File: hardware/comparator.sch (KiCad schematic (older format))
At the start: 11 parts

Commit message: more work on tdr schematic
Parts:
- U?: symbol synth_lib:SY89321L -> tdr-rescue:SY89321L-synth_lib
- U?: symbol synth_lib:ADCMP580 -> tdr-rescue:ADCMP580-synth_lib
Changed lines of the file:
@@
 $EndDescr
 $Comp
-L synth_lib:ADCMP580 U?
+L tdr-rescue:ADCMP580-synth_lib U?
 U 1 1 5BC42930
 P 5200 3300
@@
 	5250 3950 5250 4600
 $Comp
-L synth_lib:SY89321L U?
+L tdr-rescue:SY89321L-synth_lib U?
 U 1 1 5BC3E45C
 P 8650 3300

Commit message: work on tdr schematic..
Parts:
- U?: symbol tdr-rescue:SY89321L-synth_lib -> tdr-rescue:SY89321L-synth_lib-tdr-rescue
- U?: symbol tdr-rescue:ADCMP580-synth_lib -> tdr-rescue:ADCMP580-synth_lib-tdr-rescue
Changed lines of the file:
@@
 $Descr A4 11693 8268
 encoding utf-8
-Sheet 4 9
+Sheet 4 8
 Title ""
 Date ""
@@
 $EndDescr
 $Comp
-L tdr-rescue:ADCMP580-synth_lib U?
+L tdr-rescue:ADCMP580-synth_lib-tdr-rescue U?
 U 1 1 5BC42930
 P 5200 3300
@@
 	5250 3950 5250 4600
 $Comp
-L tdr-rescue:SY89321L-synth_lib U?
+L tdr-rescue:SY89321L-synth_lib-tdr-rescue U?
 U 1 1 5BC3E45C
 P 8650 3300

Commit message: footprint assignment
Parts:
- C401, C402, C403, C404, C405: renamed from C?; footprint (none) -> Capacitors_SMD:C_0402
- R401, R402, R403, R404: renamed from R?; footprint (none) -> Resistors_SMD:R_0402
- U401: renamed from U?; footprint (none) -> Housings_DFN_QFN:QFN-16-1EP_3x3mm_Pitch0.5mm
- U402: renamed from U?; footprint (none) -> Housings_DFN_QFN:DFN-8-1EP_2x2mm_Pitch0.5mm
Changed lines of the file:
@@
 $EndDescr
 $Comp
-L tdr-rescue:ADCMP580-synth_lib-tdr-rescue U?
+L tdr-rescue:ADCMP580-synth_lib-tdr-rescue U401
 U 1 1 5BC42930
 P 5200 3300
-F 0 "U?" H 4500 3900 50  0000 L CNN
+F 0 "U401" H 4500 3900 50  0000 L CNN
 F 1 "ADCMP580" H 4500 3800 50  0000 L CNN
-F 2 "" H 4300 3800 50  0001 C CNN
+F 2 "Housings_DFN_QFN:QFN-16-1EP_3x3mm_Pitch0.5mm" H 4300 3800 50  0001 C CNN
 F 3 "" H 4300 3800 50  0001 C CNN
 	1    5200 3300
@@
 $EndComp
 $Comp
-L power:+5VA #PWR?
+L power:+5VA #PWR0211
 U 1 1 5BC42937
 P 5050 2100
-F 0 "#PWR?" H 5050 1950 50  0001 C CNN
+F 0 "#PWR0211" H 5050 1950 50  0001 C CNN
 F 1 "+5VA" V 5050 2350 50  0000 C CNN
 F 2 "" H 5050 2100 50  0001 C CNN
@@
 $EndComp
 $Comp
-L power:-5VA #PWR?
+L power:-5VA #PWR0212
 U 1 1 5BC4293D
 P 5350 2100
-F 0 "#PWR?" H 5350 2200 50  0001 C CNN
+F 0 "#PWR0212" H 5350 2200 50  0001 C CNN
 F 1 "-5VA" H 5365 2273 50  0000 C CNN
 F 2 "" H 5350 2100 50  0001 C CNN
@@
 $EndComp
 $Comp
-L power:GND #PWR?
+L power:GND #PWR0213
 U 1 1 5BC42943
 P 5350 4000
-F 0 "#PWR?" H 5350 3750 50  0001 C CNN
+F 0 "#PWR0213" H 5350 3750 50  0001 C CNN
 F 1 "GND" H 5355 3827 50  0000 C CNN
 F 2 "" H 5350 4000 50  0001 C CNN
@@
 	5350 3950 5350 4000
 $Comp
-L power:GND #PWR?
+L power:GND #PWR0214
 U 1 1 5BC4294A
 P 5450 4000
-F 0 "#PWR?" H 5450 3750 50  0001 C CNN
+F 0 "#PWR0214" H 5450 3750 50  0001 C CNN
 F 1 "GND" H 5455 3827 50  0000 C CNN
 F 2 "" H 5450 4000 50  0001 C CNN
@@
 	5450 4000 5450 3950
 $Comp
-L power:GND #PWR?
+L power:GND #PWR0215
 U 1 1 5BC42951
 P 5900 3450
-F 0 "#PWR?" H 5900 3200 50  0001 C CNN
+F 0 "#PWR0215" H 5900 3200 50  0001 C CNN
 F 1 "GND" V 5905 3322 50  0000 R CNN
 F 2 "" H 5900 3450 50  0001 C CNN
@@
 	5900 3450 5850 3450
 $Comp
-L power:GND #PWR?
+L power:GND #PWR0216
 U 1 1 5BC42958
 P 5900 3150
-F 0 "#PWR?" H 5900 2900 50  0001 C CNN
+F 0 "#PWR0216" H 5900 2900 50  0001 C CNN
 F 1 "GND" V 5905 3022 50  0000 R CNN
 F 2 "" H 5900 3150 50  0001 C CNN
@@
 	5900 3150 5850 3150
 $Comp
-L power:GND #PWR?
+L power:GND #PWR0217
 U 1 1 5BC4295F
 P 5150 2600
-F 0 "#PWR?" H 5150 2350 50  0001 C CNN
+F 0 "#PWR0217" H 5150 2350 50  0001 C CNN
 F 1 "GND" V 5200 2600 50  0001 C CNN
 F 2 "" H 5150 2600 50  0001 C CNN
@@
 $EndComp
 $Comp
-L Device:C_Small C?
+L Device:C_Small C401
 U 1 1 5BC42965
 P 4750 2350
-F 0 "C?" H 4350 2400 50  0000 L CNN
+F 0 "C401" H 4350 2400 50  0000 L CNN
 F 1 ".01 uF" H 4350 2300 50  0000 L CNN
-F 2 "" H 4750 2350 50  0001 C CNN
+F 2 "Capacitors_SMD:C_0402" H 4750 2350 50  0001 C CNN
 F 3 "~" H 4750 2350 50  0001 C CNN
 	1    4750 2350
@@
 	5050 2200 5050 2650
 $Comp
-L power:GND #PWR?
+L power:GND #PWR0218
 U 1 1 5BC42971
 P 4750 2500
-F 0 "#PWR?" H 4750 2250 50  0001 C CNN
+F 0 "#PWR0218" H 4750 2250 50  0001 C CNN
 F 1 "GND" H 4750 2350 50  0000 C CNN
 F 2 "" H 4750 2500 50  0001 C CNN
@@
 	4750 2500 4750 2450
 $Comp
-L power:+5VA #PWR?
+L power:+5VA #PWR0219
 U 1 1 5BC42978
 P 4700 4050
-F 0 "#PWR?" H 4700 3900 50  0001 C CNN
+F 0 "#PWR0219" H 4700 3900 50  0001 C CNN
 F 1 "+5VA" V 4700 4300 50  0000 C CNN
 F 2 "" H 4700 4050 50  0001 C CNN
@@
 	5050 4050 4800 4050
 $Comp
-L Device:C_Small C?
+L Device:C_Small C402
 U 1 1 5BC42980
 P 4800 4200
-F 0 "C?" H 4892 4246 50  0000 L CNN
+F 0 "C402" H 4892 4246 50  0000 L CNN
 F 1 ".01 uF" H 4892 4155 50  0000 L CNN
-F 2 "" H 4800 4200 50  0001 C CNN
+F 2 "Capacitors_SMD:C_0402" H 4800 4200 50  0001 C CNN
 F 3 "~" H 4800 4200 50  0001 C CNN
 	1    4800 4200
@@
 $EndComp
 $Comp
-L power:GND #PWR?
+L power:GND #PWR0220
 U 1 1 5BC42987
 P 4800 4350
-F 0 "#PWR?" H 4800 4100 50  0001 C CNN
+F 0 "#PWR0220" H 4800 4100 50  0001 C CNN
 F 1 "GND" H 4800 4200 50  0000 C CNN
 F 2 "" H 4800 4350 50  0001 C CNN
@@
 	4800 4050 4700 4050
 $Comp
-L Device:R_Small R?
+L Device:R_Small R403
 U 1 1 5BC42991
 P 5250 2300
-F 0 "R?" V 5150 2350 50  0000 L CNN
+F 0 "R403" V 5150 2350 50  0000 L CNN
 F 1 "TBD" V 5150 2150 50  0000 L CNN
-F 2 "" H 5250 2300 50  0001 C CNN
+F 2 "Resistors_SMD:R_0402" H 5250 2300 50  0001 C CNN
 F 3 "~" H 5250 2300 50  0001 C CNN
 	1    5250 2300
@@
 $EndComp
 $Comp
-L power:GND #PWR?
+L power:GND #PWR0221
 U 1 1 5BC42998
 P 5250 2100
-F 0 "#PWR?" H 5250 1850 50  0001 C CNN
+F 0 "#PWR0221" H 5250 1850 50  0001 C CNN
 F 1 "GND" V 5250 1850 50  0000 C CNN
 F 2 "" H 5250 2100 50  0001 C CNN
@@
 	5350 2100 5350 2200
 $Comp
-L Device:C_Small C?
+L Device:C_Small C403
 U 1 1 5BC429A1
 P 5600 2350
-F 0 "C?" H 5692 2396 50  0000 L CNN
+F 0 "C403" H 5692 2396 50  0000 L CNN
 F 1 ".01 uF" H 5692 2305 50  0000 L CNN
-F 2 "" H 5600 2350 50  0001 C CNN
+F 2 "Capacitors_SMD:C_0402" H 5600 2350 50  0001 C CNN
 F 3 "~" H 5600 2350 50  0001 C CNN
 	1    5600 2350
@@
 $EndComp
 $Comp
-L power:GND #PWR?
+L power:GND #PWR0222
 U 1 1 5BC429A8
 P 5600 2500
-F 0 "#PWR?" H 5600 2250 50  0001 C CNN
+F 0 "#PWR0222" H 5600 2250 50  0001 C CNN
 F 1 "GND" H 5600 2350 50  0000 C CNN
 F 2 "" H 5600 2500 50  0001 C CNN
@@
 	5150 2600 5150 2650
 $Comp
-L Device:R_Small R?
+L Device:R_Small R402
 U 1 1 5BC429B4
 P 4250 3550
-F 0 "R?" V 4150 3600 50  0000 L CNN
+F 0 "R402" V 4150 3600 50  0000 L CNN
 F 1 "DNI" V 4150 3400 50  0000 L CNN
-F 2 "" H 4250 3550 50  0001 C CNN
+F 2 "Resistors_SMD:R_0402" H 4250 3550 50  0001 C CNN
 F 3 "~" H 4250 3550 50  0001 C CNN
 	1    4250 3550
@@
 $EndComp
 $Comp
-L Device:R_Small R?
+L Device:R_Small R401
 U 1 1 5BC429BB
 P 4250 3100
-F 0 "R?" V 4150 3150 50  0000 L CNN
+F 0 "R401" V 4150 3150 50  0000 L CNN
 F 1 "JMP" V 4150 2950 50  0000 L CNN
-F 2 "" H 4250 3100 50  0001 C CNN
+F 2 "Resistors_SMD:R_0402" H 4250 3100 50  0001 C CNN
 F 3 "~" H 4250 3100 50  0001 C CNN
 	1    4250 3100
@@
 	4450 3100 4350 3100
 $Comp
-L power:GND #PWR?
+L power:GND #PWR0223
 U 1 1 5BC429C4
 P 4050 3100
-F 0 "#PWR?" H 4050 2850 50  0001 C CNN
+F 0 "#PWR0223" H 4050 2850 50  0001 C CNN
 F 1 "GND" V 4100 3100 50  0001 C CNN
 F 2 "" H 4050 3100 50  0001 C CNN
@@
 	4450 3150 4550 3150
 $Comp
-L power:GND #PWR?
+L power:GND #PWR0224
 U 1 1 5BC429CF
 P 4050 3550
-F 0 "#PWR?" H 4050 3300 50  0001 C CNN
+F 0 "#PWR0224" H 4050 3300 50  0001 C CNN
 F 1 "GND" V 4100 3550 50  0001 C CNN
 F 2 "" H 4050 3550 50  0001 C CNN
@@
 	5250 3950 5250 4600
 $Comp
-L tdr-rescue:SY89321L-synth_lib-tdr-rescue U?
+L tdr-rescue:SY89321L-synth_lib-tdr-rescue U402
 U 1 1 5BC3E45C
 P 8650 3300
-F 0 "U?" H 8650 3715 50  0000 C CNN
+F 0 "U402" H 8650 3715 50  0000 C CNN
 F 1 "SY89321L" H 8650 3624 50  0000 C CNN
-F 2 "" H 8550 3300 50  0001 C CNN
+F 2 "Housings_DFN_QFN:DFN-8-1EP_2x2mm_Pitch0.5mm" H 8550 3300 50  0001 C CNN
 F 3 "" H 8550 3300 50  0001 C CNN
 	1    8650 3300
@@
 $EndComp
 $Comp
-L Device:R_Small R?
+L Device:R_Small R404
 U 1 1 5BC3F0C6
 P 7750 3300
-F 0 "R?" V 7650 3350 50  0000 L CNN
+F 0 "R404" V 7650 3350 50  0000 L CNN
 F 1 "100" V 7650 3150 50  0000 L CNN
-F 2 "" H 7750 3300 50  0001 C CNN
+F 2 "Resistors_SMD:R_0402" H 7750 3300 50  0001 C CNN
 F 3 "~" H 7750 3300 50  0001 C CNN
 	1    7750 3300
@@
 	7750 3450 7900 3450
 $Comp
-L power:+3V3 #PWR?
+L power:+3V3 #PWR0225
 U 1 1 5BC41D98
 P 9250 2700
-F 0 "#PWR?" H 9250 2550 50  0001 C CNN
+F 0 "#PWR0225" H 9250 2550 50  0001 C CNN
 F 1 "+3V3" H 9265 2873 50  0000 C CNN
 F 2 "" H 9250 2700 50  0001 C CNN
@@
 	9100 3250 9850 3250
 $Comp
-L power:GND #PWR?
+L power:GND #PWR0226
 U 1 1 5BC43ABE
 P 9250 3500
-F 0 "#PWR?" H 9250 3250 50  0001 C CNN
+F 0 "#PWR0226" H 9250 3250 50  0001 C CNN
 F 1 "GND" V 9255 3372 50  0000 R CNN
 F 2 "" H 9250 3500 50  0001 C CNN
@@
 	9250 2700 9250 2750
 $Comp
-L Device:C_Small C?
+L Device:C_Small C405
 U 1 1 5BC45A33
 P 9400 2900
-F 0 "C?" H 9550 2950 50  0000 L CNN
+F 0 "C405" H 9550 2950 50  0000 L CNN
 F 1 ".01 uF" H 9550 2850 50  0000 L CNN
-F 2 "" H 9400 2900 50  0001 C CNN
+F 2 "Capacitors_SMD:C_0402" H 9400 2900 50  0001 C CNN
 F 3 "~" H 9400 2900 50  0001 C CNN
 	1    9400 2900
@@
 $EndComp
 $Comp
-L power:GND #PWR?
+L power:GND #PWR0227
 U 1 1 5BC46600
 P 9400 3050
-F 0 "#PWR?" H 9400 2800 50  0001 C CNN
+F 0 "#PWR0227" H 9400 2800 50  0001 C CNN
 F 1 "GND" V 9405 2922 50  0001 R CNN
 F 2 "" H 9400 3050 50  0001 C CNN
@@
 	9400 3000 9400 3050
 $Comp
-L power:GND #PWR?
+L power:GND #PWR0228
 U 1 1 5BC47E75
 P 8650 3900
-F 0 "#PWR?" H 8650 3650 50  0001 C CNN
+F 0 "#PWR0228" H 8650 3650 50  0001 C CNN
 F 1 "GND" V 8655 3772 50  0000 R CNN
 F 2 "" H 8650 3900 50  0001 C CNN
@@
 	8650 3800 8650 3900
 $Comp
-L Device:C_Small C?
+L Device:C_Small C404
 U 1 1 5BC48B4A
 P 8050 3750
-F 0 "C?" H 8150 3800 50  0000 L CNN
+F 0 "C404" H 8150 3800 50  0000 L CNN
 F 1 "DNP" H 8150 3700 50  0000 L CNN
-F 2 "" H 8050 3750 50  0001 C CNN
+F 2 "Capacitors_SMD:C_0402" H 8050 3750 50  0001 C CNN
 F 3 "~" H 8050 3750 50  0001 C CNN
 	1    8050 3750
@@
 	8050 3450 8050 3650
 $Comp
-L power:+3V3 #PWR?
+L power:+3V3 #PWR0229
 U 1 1 5BC4B212
 P 8050 3900
-F 0 "#PWR?" H 8050 3750 50  0001 C CNN
+F 0 "#PWR0229" H 8050 3750 50  0001 C CNN
 F 1 "+3V3" H 8065 4073 50  0000 C CNN
 F 2 "" H 8050 3900 50  0001 C CNN

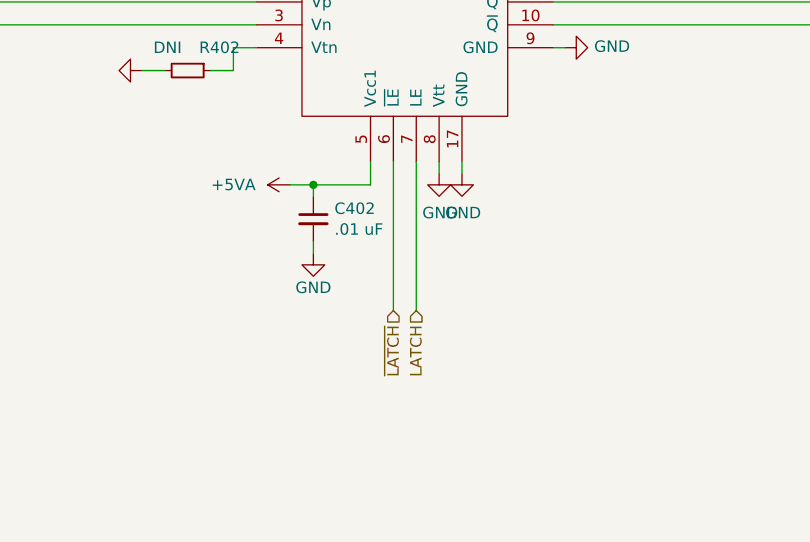
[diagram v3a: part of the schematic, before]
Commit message: work on tdr component placement
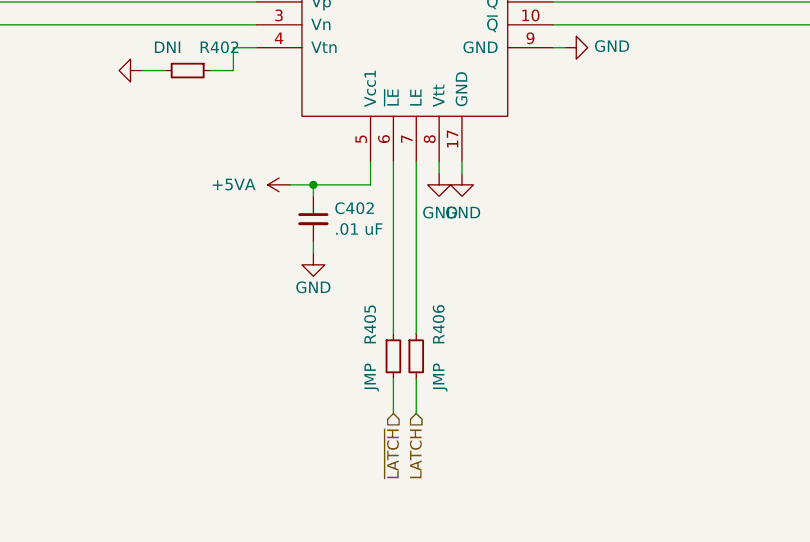
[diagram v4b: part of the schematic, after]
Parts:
- added R405, R406: JMP, Resistors_SMD:R_0402, symbol Device:R_Small
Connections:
- net LATCH: now also R406.2; no longer U401.7 (LE)
- net ~LATCH: now also R405.2; no longer U401.6 (~LE)
- new net: R405.1, U401.6 (~LE)
- new net: R406.1, U401.7 (LE)
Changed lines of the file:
@@
 Text HLabel 3250 3350 0    50   Input ~ 0
 REF_INPUT
-Text HLabel 5150 4600 3    50   Input ~ 0
+Text HLabel 5150 5050 3    50   Input ~ 0
 ~LATCH
-Text HLabel 5250 4600 3    50   Input ~ 0
+Text HLabel 5250 5050 3    50   Input ~ 0
 LATCH
-Wire Wire Line
-	5150 4600 5150 3950
-Wire Wire Line
-	5250 3950 5250 4600
 $Comp
 L tdr-rescue:SY89321L-synth_lib-tdr-rescue U402
@@
 Text Notes 2950 3150 0    50   ~ 0
 +/- 2V
+$Comp
+L Device:R_Small R405
+U 1 1 5C37AFC8
+P 5150 4800
+F 0 "R405" V 5050 4850 50  0000 L CNN
+F 1 "JMP" V 5050 4650 50  0000 L CNN
+F 2 "Resistors_SMD:R_0402" H 5150 4800 50  0001 C CNN
+F 3 "~" H 5150 4800 50  0001 C CNN
+	1    5150 4800
+	1    0    0    -1
+$EndComp
+$Comp
+L Device:R_Small R406
+U 1 1 5C37B0A4
+P 5250 4800
+F 0 "R406" V 5350 4850 50  0000 L CNN
+F 1 "JMP" V 5350 4650 50  0000 L CNN
+F 2 "Resistors_SMD:R_0402" H 5250 4800 50  0001 C CNN
+F 3 "~" H 5250 4800 50  0001 C CNN
+	1    5250 4800
+	1    0    0    -1
+$EndComp
+Wire Wire Line
+	5250 3950 5250 4700
+Wire Wire Line
+	5150 3950 5150 4700
+Wire Wire Line
+	5150 4900 5150 5050
+Wire Wire Line
+	5250 4900 5250 5050
 $EndSCHEMATC

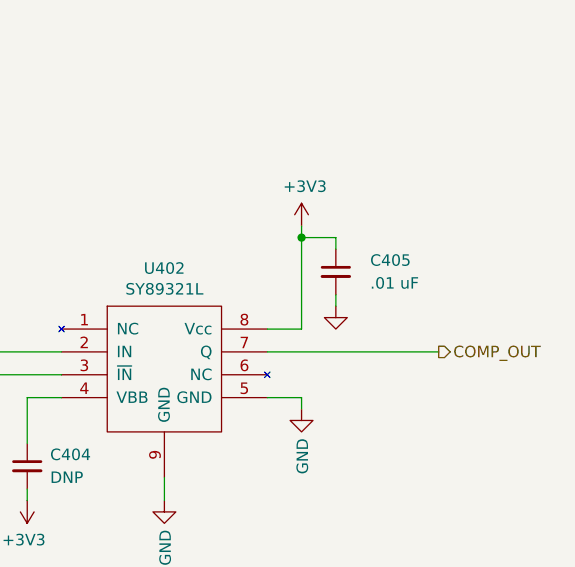
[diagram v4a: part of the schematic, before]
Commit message: more component placement on tdr..
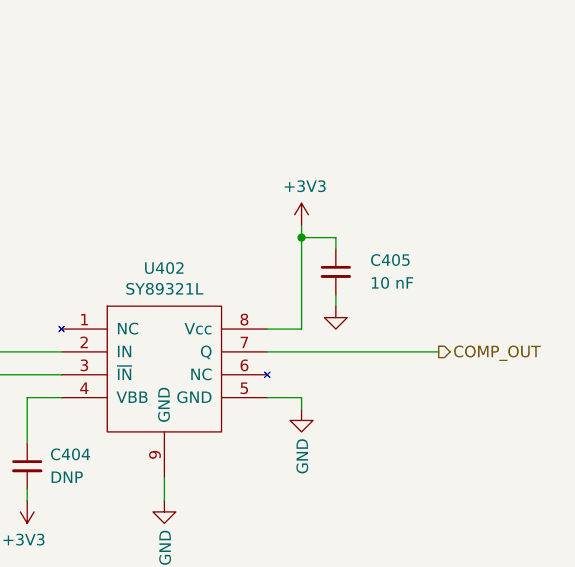
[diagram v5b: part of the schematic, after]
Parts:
- C405: value .01 uF -> 10 nF
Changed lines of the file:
@@
 P 9400 2900
 F 0 "C405" H 9550 2950 50  0000 L CNN
-F 1 ".01 uF" H 9550 2850 50  0000 L CNN
+F 1 "10 nF" H 9550 2850 50  0000 L CNN
 F 2 "Capacitors_SMD:C_0402" H 9400 2900 50  0001 C CNN
 F 3 "~" H 9400 2900 50  0001 C CNN

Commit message: first pass of layout complete
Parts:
- U402: footprint Housings_DFN_QFN:DFN-8-1EP_2x2mm_Pitch0.5mm -> vna_footprints:DFN-8-1EP_2x2mm_Pitch0.5mm
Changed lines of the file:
@@
 F 0 "U402" H 8650 3715 50  0000 C CNN
 F 1 "SY89321L" H 8650 3624 50  0000 C CNN
-F 2 "Housings_DFN_QFN:DFN-8-1EP_2x2mm_Pitch0.5mm" H 8550 3300 50  0001 C CNN
+F 2 "vna_footprints:DFN-8-1EP_2x2mm_Pitch0.5mm" H 8550 3300 50  0001 C CNN
 F 3 "" H 8550 3300 50  0001 C CNN
 	1    8650 3300

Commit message: fixed CML termination.. ready to order?
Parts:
- added C406: 2.2 uF, Capacitors_SMD:C_0603, symbol Device:C_Small
- added R407, R408: JMP, Resistors_SMD:R_0402, symbol Device:R_Small
- C401, C402, C403: value .01 uF -> 10 nF
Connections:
- net +3V3: now also C406.1, R408.2
- net GND: now also C406.2, R407.2; no longer U401.8 (Vtt)
- new net: R407.1, R408.1, U401.8 (Vtt)
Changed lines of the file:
@@
 L power:GND #PWR0213
 U 1 1 5BC42943
-P 5350 4000
-F 0 "#PWR0213" H 5350 3750 50  0001 C CNN
-F 1 "GND" H 5355 3827 50  0000 C CNN
-F 2 "" H 5350 4000 50  0001 C CNN
-F 3 "" H 5350 4000 50  0001 C CNN
-	1    5350 4000
-	1    0    0    -1
-$EndComp
-Wire Wire Line
-	5350 3950 5350 4000
+P 5850 4300
+F 0 "#PWR0213" H 5850 4050 50  0001 C CNN
+F 1 "GND" H 5855 4127 50  0000 C CNN
+F 2 "" H 5850 4300 50  0001 C CNN
+F 3 "" H 5850 4300 50  0001 C CNN
+	1    5850 4300
+	0    -1   -1   0
+$EndComp
 $Comp
 L power:GND #PWR0214
@@
 P 4750 2350
 F 0 "C401" H 4350 2400 50  0000 L CNN
-F 1 ".01 uF" H 4350 2300 50  0000 L CNN
+F 1 "10 nF" H 4350 2300 50  0000 L CNN
 F 2 "Capacitors_SMD:C_0402" H 4750 2350 50  0001 C CNN
 F 3 "~" H 4750 2350 50  0001 C CNN
@@
 P 4800 4200
 F 0 "C402" H 4892 4246 50  0000 L CNN
-F 1 ".01 uF" H 4892 4155 50  0000 L CNN
+F 1 "10 nF" H 4892 4155 50  0000 L CNN
 F 2 "Capacitors_SMD:C_0402" H 4800 4200 50  0001 C CNN
 F 3 "~" H 4800 4200 50  0001 C CNN
@@
 P 5600 2350
 F 0 "C403" H 5692 2396 50  0000 L CNN
-F 1 ".01 uF" H 5692 2305 50  0000 L CNN
+F 1 "10 nF" H 5692 2305 50  0000 L CNN
 F 2 "Capacitors_SMD:C_0402" H 5600 2350 50  0001 C CNN
 F 3 "~" H 5600 2350 50  0001 C CNN
@@
 Wire Wire Line
 	5250 4900 5250 5050
+$Comp
+L Device:R_Small R407
+U 1 1 5C34FAEE
+P 5700 4300
+F 0 "R407" V 5800 4350 50  0000 L CNN
+F 1 "JMP" V 5800 4150 50  0000 L CNN
+F 2 "Resistors_SMD:R_0402" H 5700 4300 50  0001 C CNN
+F 3 "~" H 5700 4300 50  0001 C CNN
+	1    5700 4300
+	0    -1   -1   0
+$EndComp
+Wire Wire Line
+	5850 4300 5800 4300
+Wire Wire Line
+	5600 4300 5350 4300
+Wire Wire Line
+	5350 3950 5350 4300
+Wire Wire Line
+	5350 4300 5350 4500
+Wire Wire Line
+	5350 4500 5600 4500
+Connection ~ 5350 4300
+$Comp
+L Device:R_Small R408
+U 1 1 5C356819
+P 5700 4500
+F 0 "R408" V 5800 4550 50  0000 L CNN
+F 1 "JMP" V 5800 4350 50  0000 L CNN
+F 2 "Resistors_SMD:R_0402" H 5700 4500 50  0001 C CNN
+F 3 "~" H 5700 4500 50  0001 C CNN
+	1    5700 4500
+	0    -1   -1   0
+$EndComp
+$Comp
+L power:+3V3 #PWR0245
+U 1 1 5C356953
+P 5850 4500
+F 0 "#PWR0245" H 5850 4350 50  0001 C CNN
+F 1 "+3V3" V 5865 4628 50  0000 L CNN
+F 2 "" H 5850 4500 50  0001 C CNN
+F 3 "" H 5850 4500 50  0001 C CNN
+	1    5850 4500
+	0    1    1    0
+$EndComp
+Wire Wire Line
+	5850 4500 5800 4500
+$Comp
+L Device:C_Small C406
+U 1 1 5C36E21C
+P 6050 5200
+F 0 "C406" H 5650 5250 50  0000 L CNN
+F 1 "2.2 uF" H 5650 5150 50  0000 L CNN
+F 2 "Capacitors_SMD:C_0603" H 6050 5200 50  0001 C CNN
+F 3 "~" H 6050 5200 50  0001 C CNN
+	1    6050 5200
+	1    0    0    -1
+$EndComp
+$Comp
+L power:+3V3 #PWR0147
+U 1 1 5C36E2D5
+P 6050 5050
+F 0 "#PWR0147" H 6050 4900 50  0001 C CNN
+F 1 "+3V3" H 6065 5223 50  0000 C CNN
+F 2 "" H 6050 5050 50  0001 C CNN
+F 3 "" H 6050 5050 50  0001 C CNN
+	1    6050 5050
+	1    0    0    -1
+$EndComp
+Wire Wire Line
+	6050 5100 6050 5050
+$Comp
+L power:GND #PWR0148
+U 1 1 5C370836
+P 6050 5350
+F 0 "#PWR0148" H 6050 5100 50  0001 C CNN
+F 1 "GND" H 6055 5177 50  0000 C CNN
+F 2 "" H 6050 5350 50  0001 C CNN
+F 3 "" H 6050 5350 50  0001 C CNN
+	1    6050 5350
+	1    0    0    -1
+$EndComp
+Wire Wire Line
+	6050 5300 6050 5350
 $EndSCHEMATC

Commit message: schematic cleanup, BOM consolidation
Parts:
- C406: value 2.2 uF -> 4.7 uF
- R403: value TBD -> 1k
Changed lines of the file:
@@
 P 5250 2300
 F 0 "R403" V 5150 2350 50  0000 L CNN
-F 1 "TBD" V 5150 2150 50  0000 L CNN
+F 1 "1k" V 5150 2150 50  0000 L CNN
 F 2 "Resistors_SMD:R_0402" H 5250 2300 50  0001 C CNN
 F 3 "~" H 5250 2300 50  0001 C CNN
@@
 P 6050 5200
 F 0 "C406" H 5650 5250 50  0000 L CNN
-F 1 "2.2 uF" H 5650 5150 50  0000 L CNN
+F 1 "4.7 uF" H 5650 5150 50  0000 L CNN
 F 2 "Capacitors_SMD:C_0603" H 6050 5200 50  0001 C CNN
 F 3 "~" H 6050 5200 50  0001 C CNN
